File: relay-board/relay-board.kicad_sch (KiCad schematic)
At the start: 5 parts, among them J1 Conn_01x25

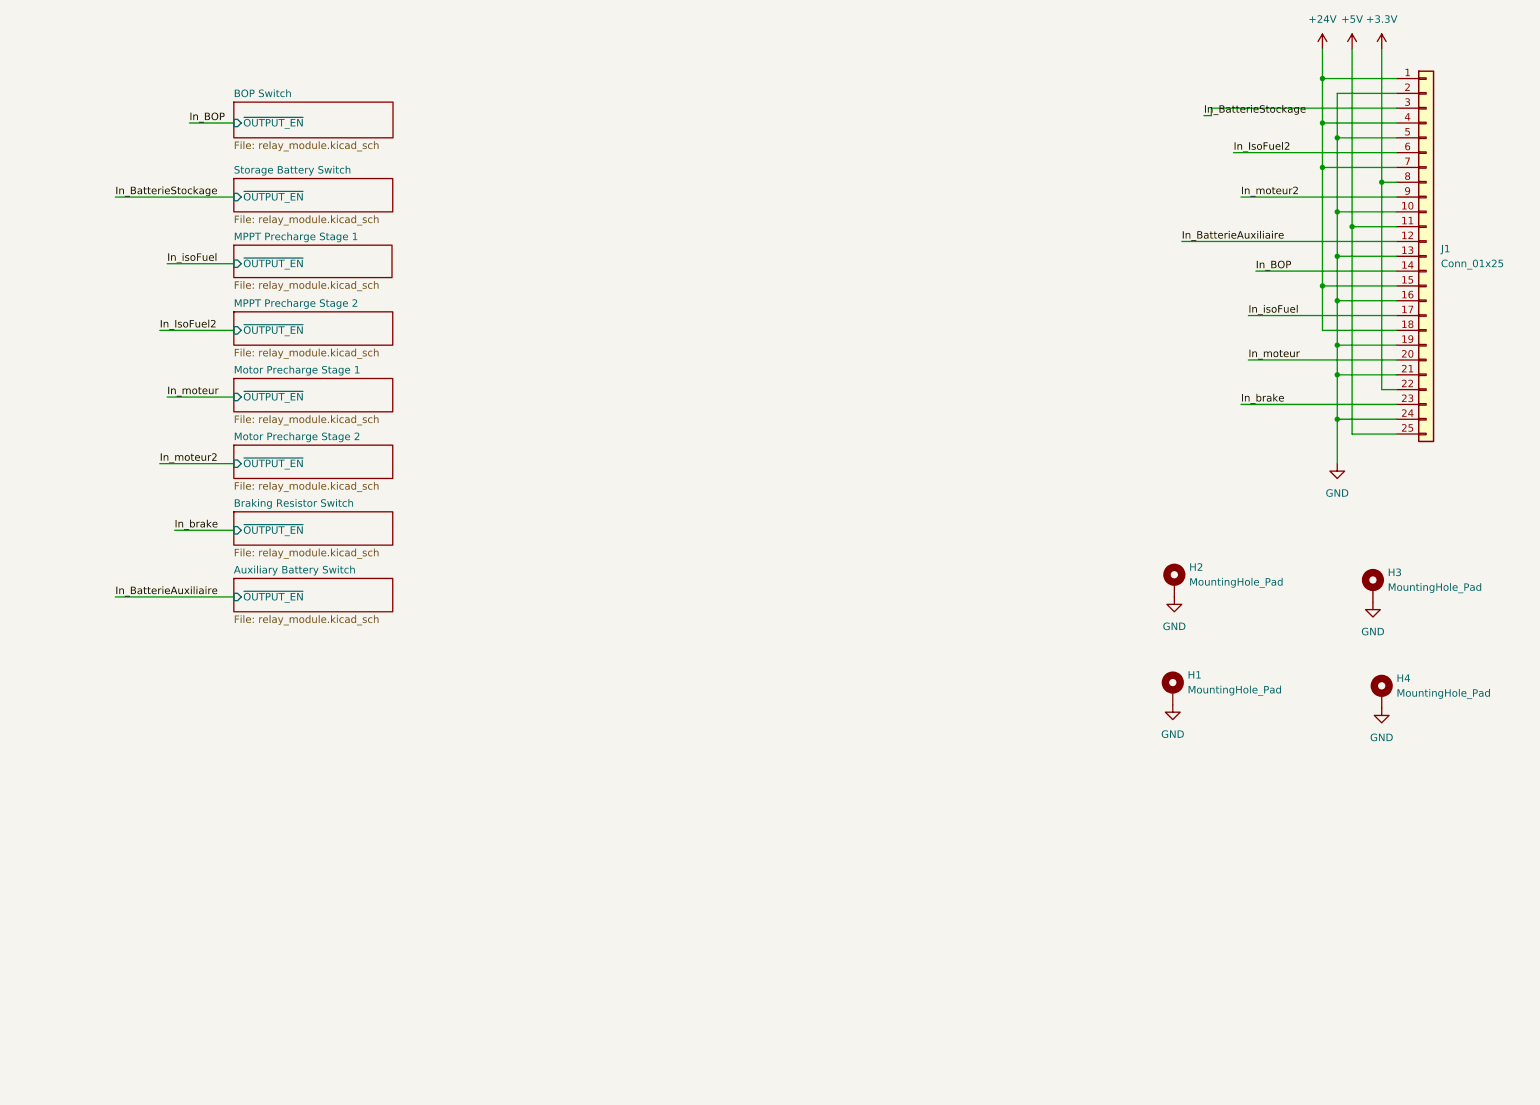
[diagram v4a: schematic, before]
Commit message: relay-board: change 25-pin connector symbol
Also fixed all ERC warnings and renamed nets to match those of the
power-pcb project.
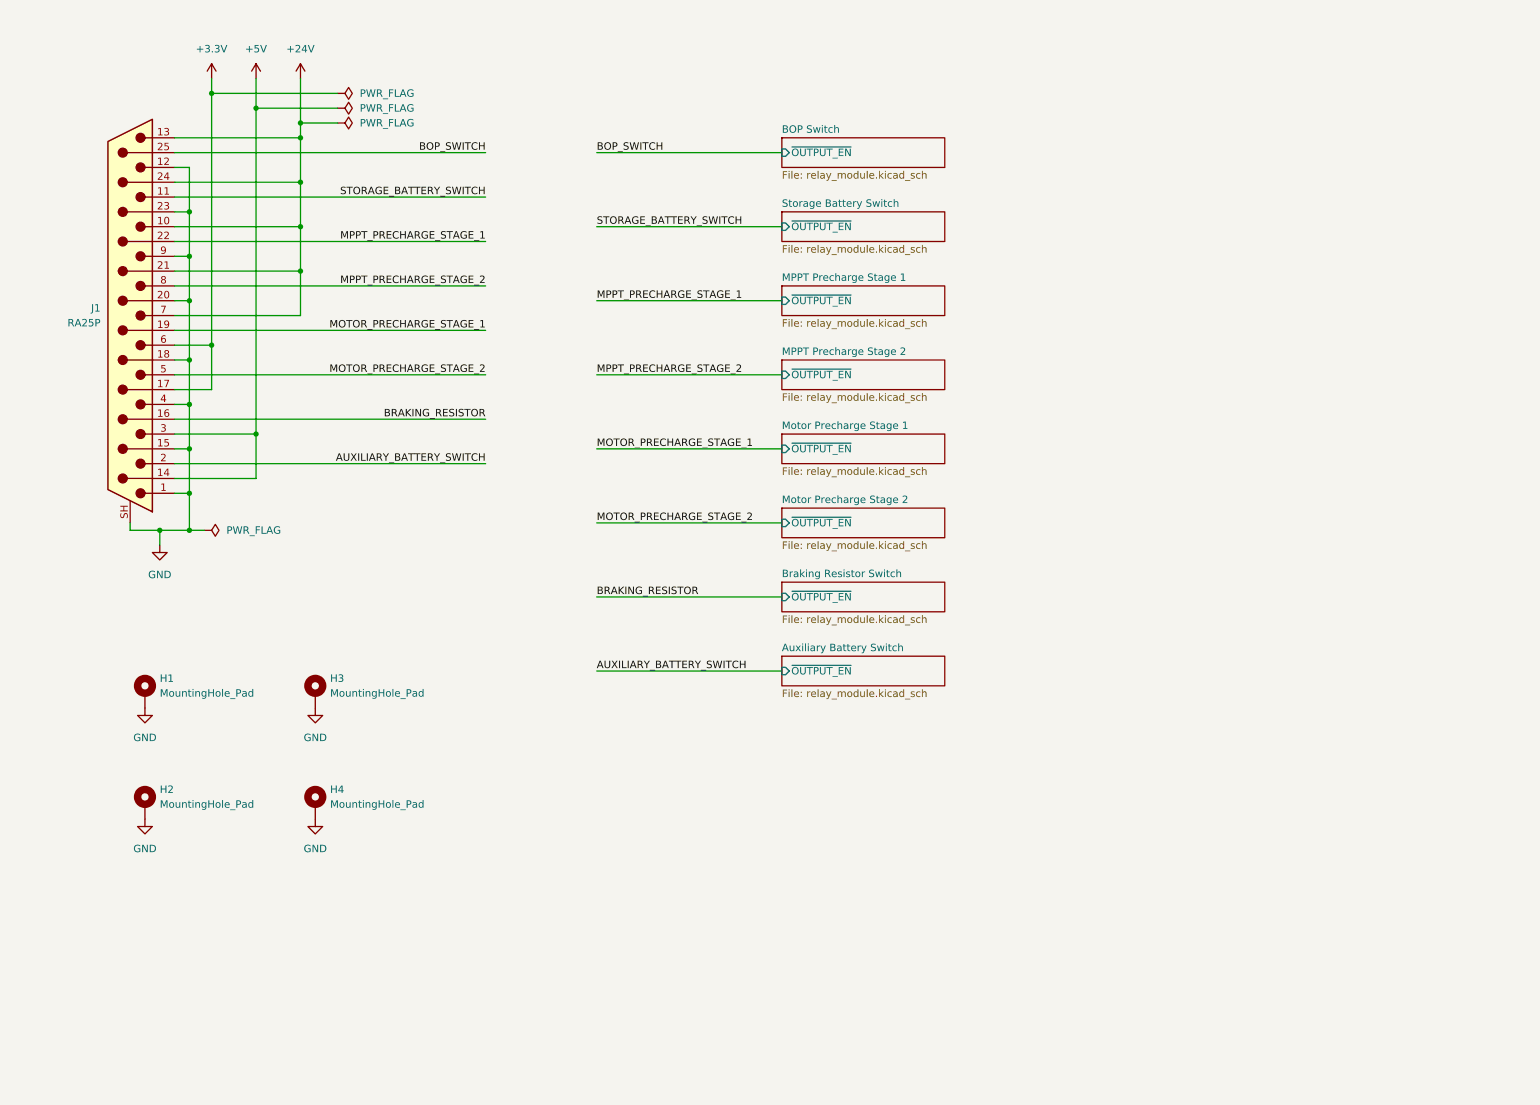
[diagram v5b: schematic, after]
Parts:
- removed J1: Conn_01x25, symbol Connector_Generic:Conn_01x25
- added J1: RA25P, Connector_Dsub:DSUB-25_Socket_Horizontal_P2.77x2.84mm_EdgePinOffset7.70mm_Housed_MountingHolesOffset9.12mm, symbol Connector:DB25_Pins_MountingHoles
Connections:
- net +24V: now also J1.10, J1.13, J1.21 (P21), J1.24 (P24), J1.7
- net +3.3V: now also J1.17 (P17), J1.6
- net +5V: now also J1.14 (P14), J1.3
- net GND: now also J1.1, J1.12, J1.15 (P15), J1.18 (P18), J1.20 (P20), J1.23 (P23), J1.4, J1.9, J1.SH (PAD)
- new net AUXILIARY_BATTERY_SWITCH: J1.2
- new net BOP_SWITCH: J1.25 (P25)
- new net BRAKING_RESISTOR: J1.16 (P16)
- new net MOTOR_PRECHARGE_STAGE_1: J1.19 (P19)
- new net MOTOR_PRECHARGE_STAGE_2: J1.5
- new net MPPT_PRECHARGE_STAGE_1: J1.22 (P22)
- new net MPPT_PRECHARGE_STAGE_2: J1.8
- new net STORAGE_BATTERY_SWITCH: J1.11
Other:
- moved on the sheet: H1, H2, H3, H4

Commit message: power-pcb: reduce optocoupler diode and add fuse
Also added a connector to select the source of for the 24-V net
going into the contactor coils.

Reducing the value of the resistor will ensure there is enough current
to close the 5V relay.
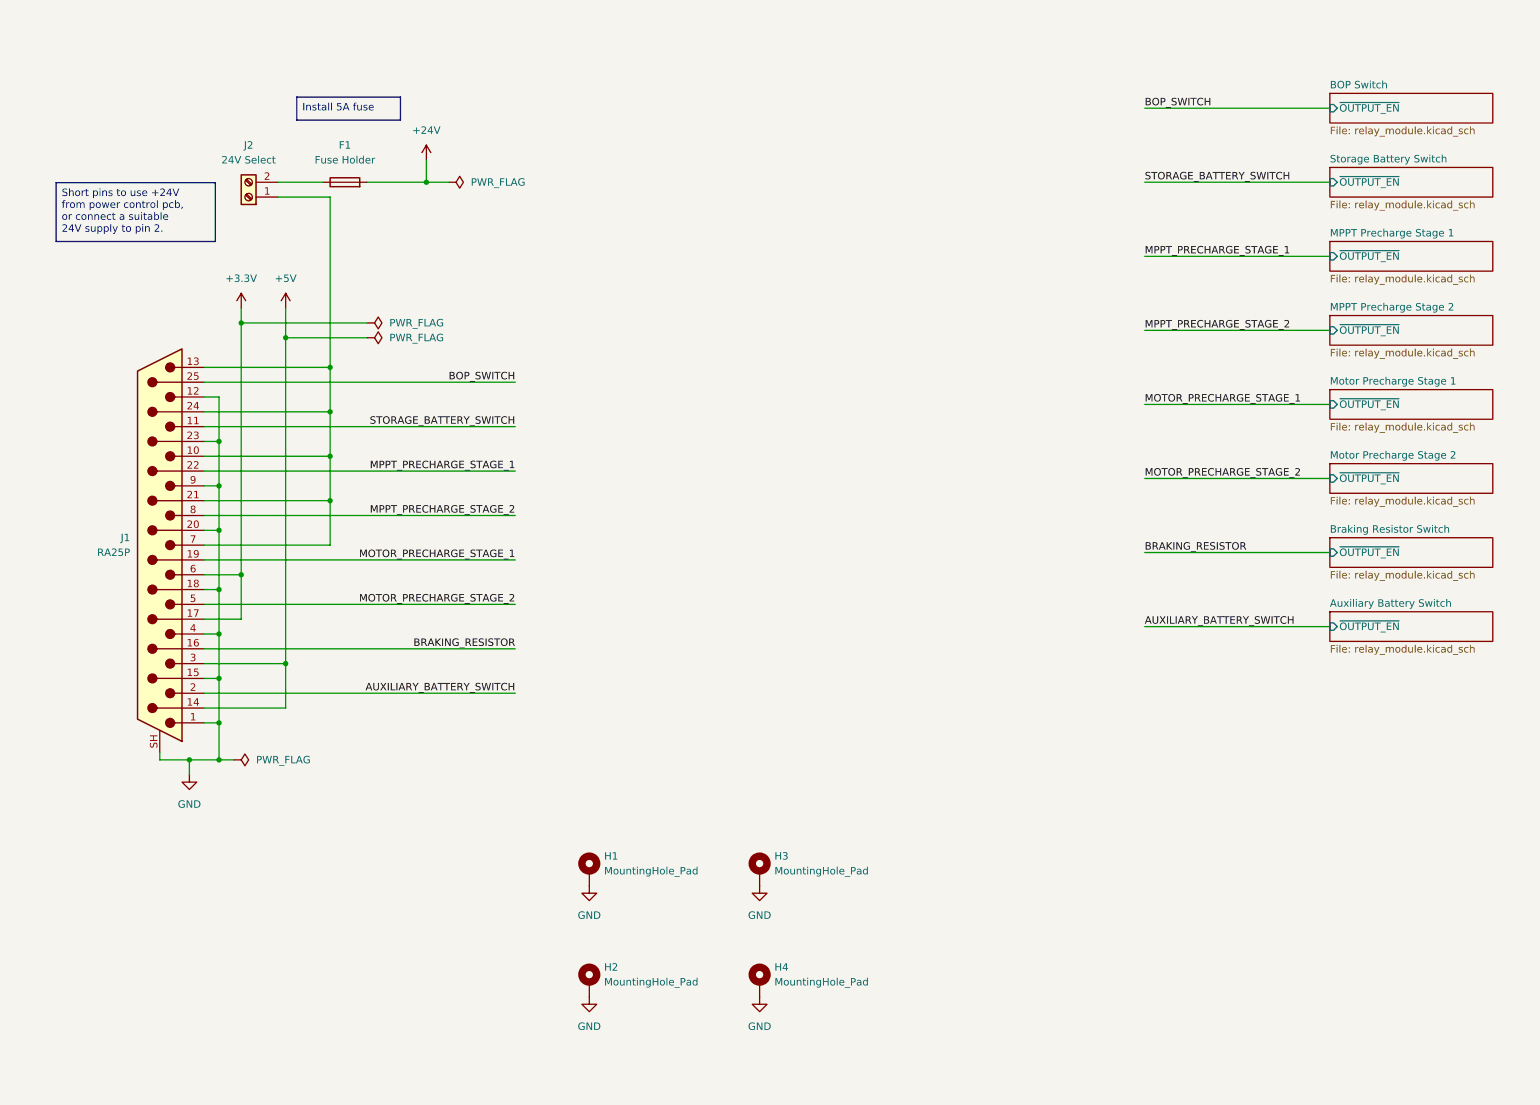
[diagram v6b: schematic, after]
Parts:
- added F1: Fuse Holder, Fuse:Fuseholder_Clip-5x20mm_Littelfuse_111_Lateral_P18.80x5.00mm_D1.17mm_Horizontal, symbol Device:Fuse
- added J2: 24V Select, Exocet:Wurth_Term_Blk_2pos_Side_Entry_5mm, symbol Connector:Screw_Terminal_01x02
- J1: footprint Connector_Dsub:DSUB-25_Socket_Horizontal_P2.77x2.84mm_EdgePinOffset7.70mm_Housed_MountingHolesOffset9.12mm -> Connector_Dsub:DSUB-25_Pins_Horizontal_P2.77x2.84mm_EdgePinOffset7.70mm_Housed_MountingHolesOffset9.12mm
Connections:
- net +24V: now also F1.2; no longer J1.10, J1.13, J1.21 (P21), J1.24 (P24), J1.7
- new net: J1.10, J1.13, J1.21 (P21), J1.24 (P24), J1.7, J2.1 (Pin_1)
- new net: F1.1, J2.2 (Pin_2)
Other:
- moved on the sheet: H1, H2, H3, H4, J1

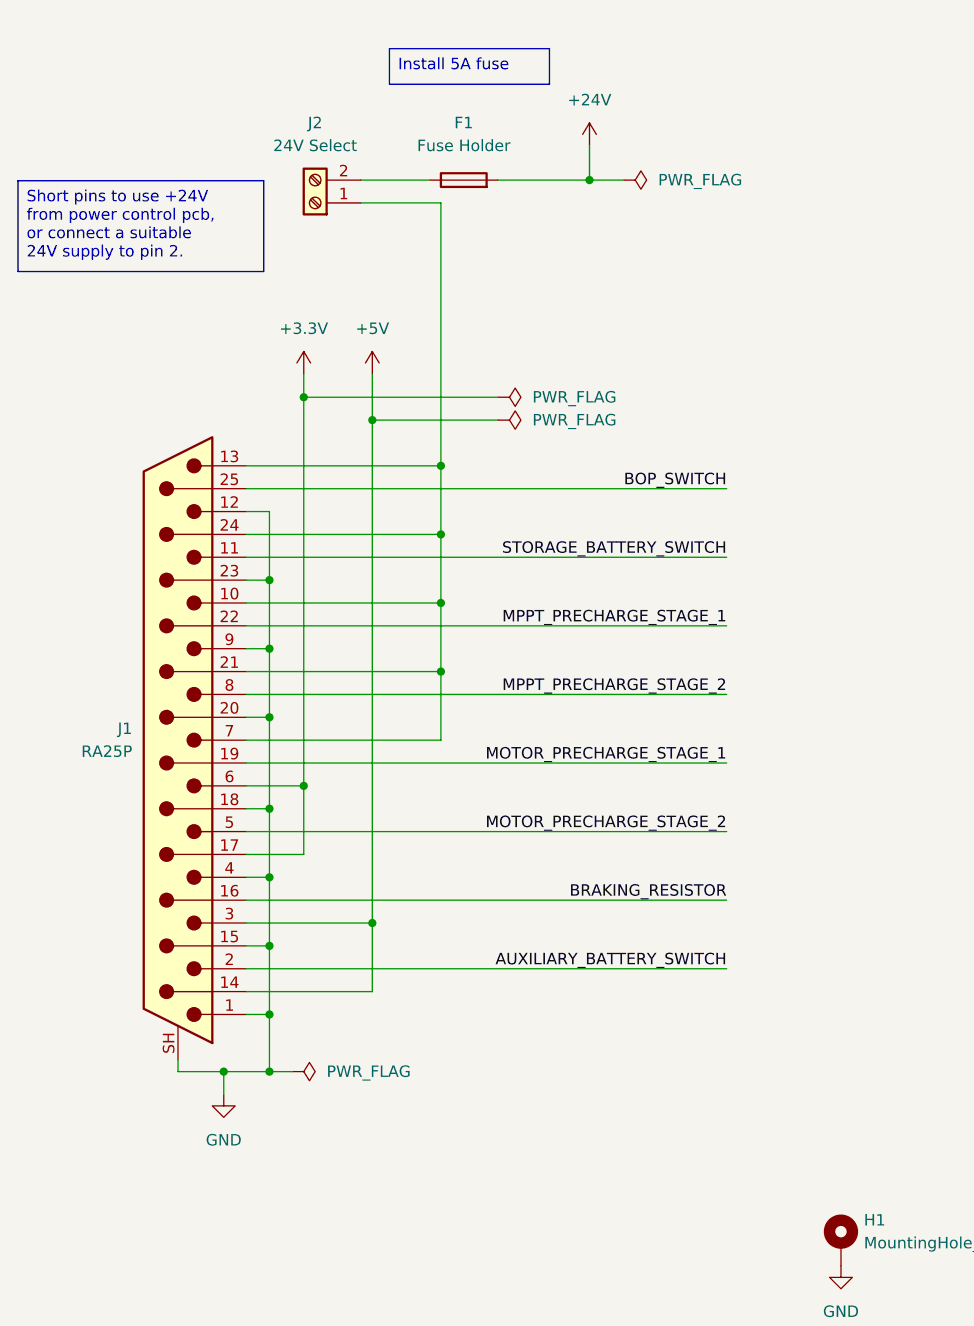
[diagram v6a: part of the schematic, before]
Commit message: relay-board: finish routing pcb
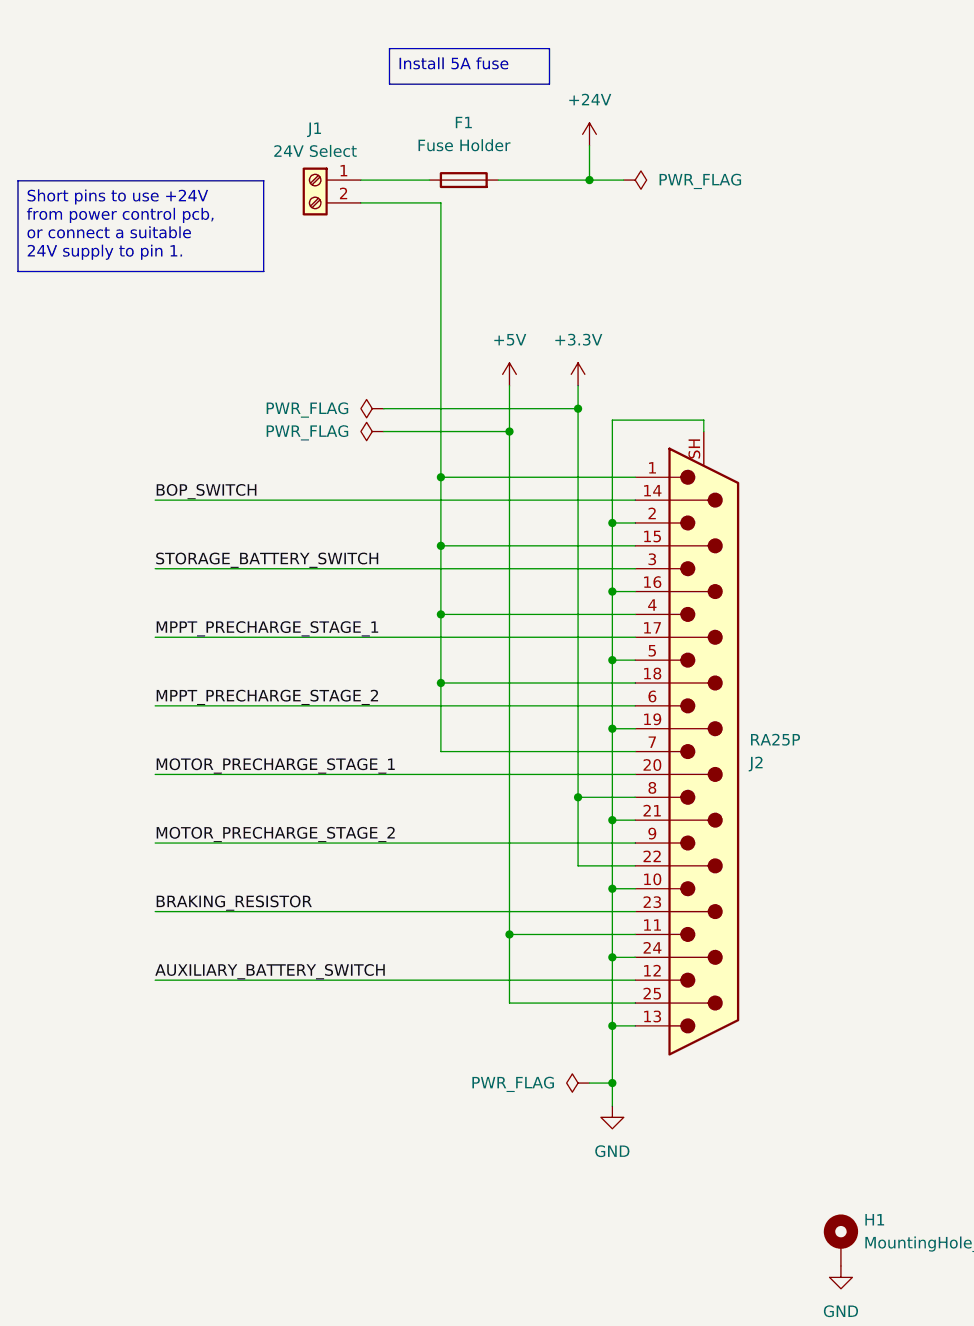
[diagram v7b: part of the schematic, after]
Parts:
- removed J1: RA25P, Connector_Dsub:DSUB-25_Pins_Horizontal_P2.77x2.84mm_EdgePinOffset7.70mm_Housed_MountingHolesOffset9.12mm, symbol Connector:DB25_Pins_MountingHoles
- removed J2: 24V Select, Exocet:Wurth_Term_Blk_2pos_Side_Entry_5mm, symbol Connector:Screw_Terminal_01x02
- added J1: 24V Select, Exocet:Wurth_Term_Blk_2pos_Side_Entry_5mm, symbol Connector:Screw_Terminal_01x02
- added J2: RA25P, Connector_Dsub:DSUB-25_Pins_Horizontal_P2.77x2.84mm_EdgePinOffset7.70mm_Housed_MountingHolesOffset9.12mm, symbol Connector:DB25_Pins_MountingHoles
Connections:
- net +3.3V: now also J2.22 (P22), J2.8
- net +5V: now also J2.11, J2.25 (P25)
- net AUXILIARY_BATTERY_SWITCH: now also J2.12
- net BOP_SWITCH: now also J2.14 (P14)
- net BRAKING_RESISTOR: now also J2.23 (P23)
- net GND: now also J2.10, J2.13, J2.16 (P16), J2.19 (P19), J2.2, J2.21 (P21), J2.24 (P24), J2.5, J2.SH (PAD)
- net MOTOR_PRECHARGE_STAGE_1: now also J2.20 (P20)
- net MOTOR_PRECHARGE_STAGE_2: now also J2.9
- net MPPT_PRECHARGE_STAGE_1: now also J2.17 (P17)
- net MPPT_PRECHARGE_STAGE_2: now also J2.6
- net STORAGE_BATTERY_SWITCH: now also J2.3
- net at F1.1: now also J1.1 (Pin_1)
- new net: J1.2 (Pin_2), J2.1, J2.15 (P15), J2.18 (P18), J2.4, J2.7
